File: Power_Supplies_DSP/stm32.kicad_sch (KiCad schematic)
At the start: 47 parts, among them J1 PINHD_1x10_Male, J2 SBH11-PBPC-D10-ST-BK, J4 PINHD_1x10_Male, J5 PINHD_1x2_Female, J6 PINHD_1x10_Female, U2 STM32H755ZIT6, U3 PEC11R-4030F-N0024, X3 NX3215SA-32.768K, X4 NX2016SA-32MHZ

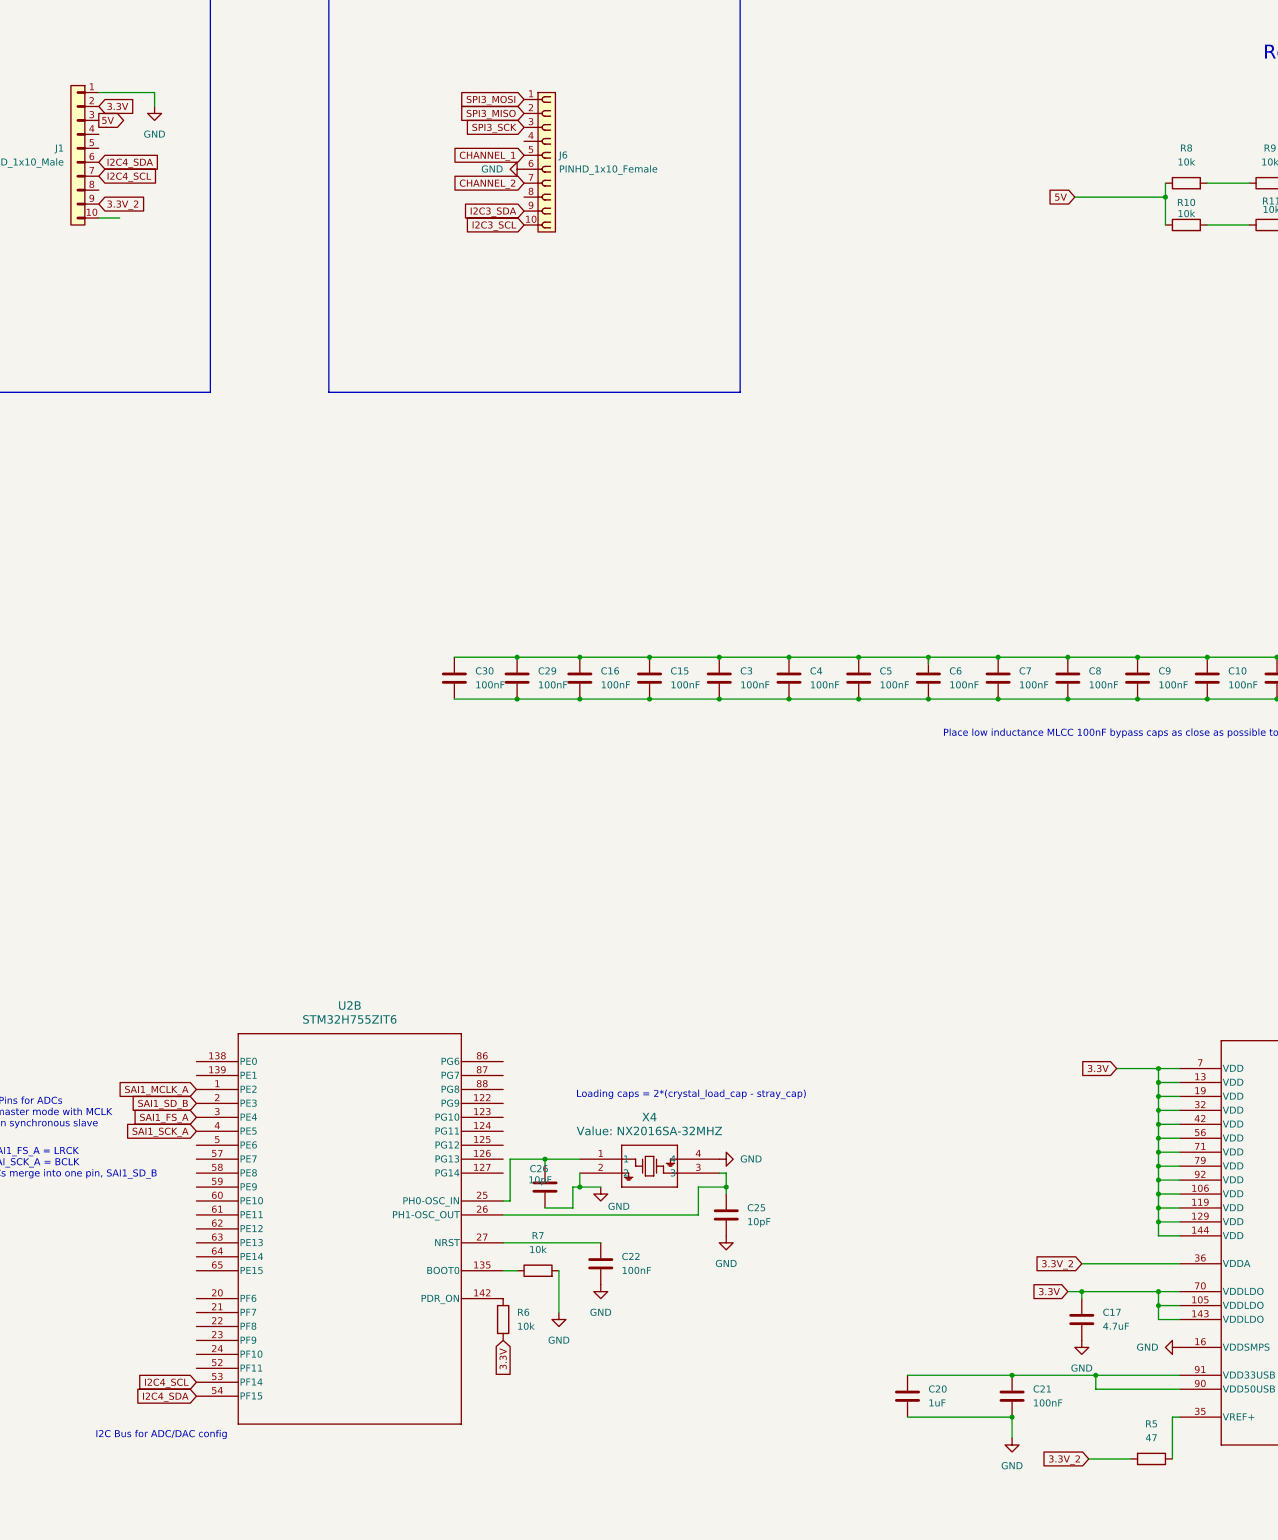
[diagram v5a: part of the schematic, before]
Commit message: fixed an oopsie w/ 3.3V on mcu board
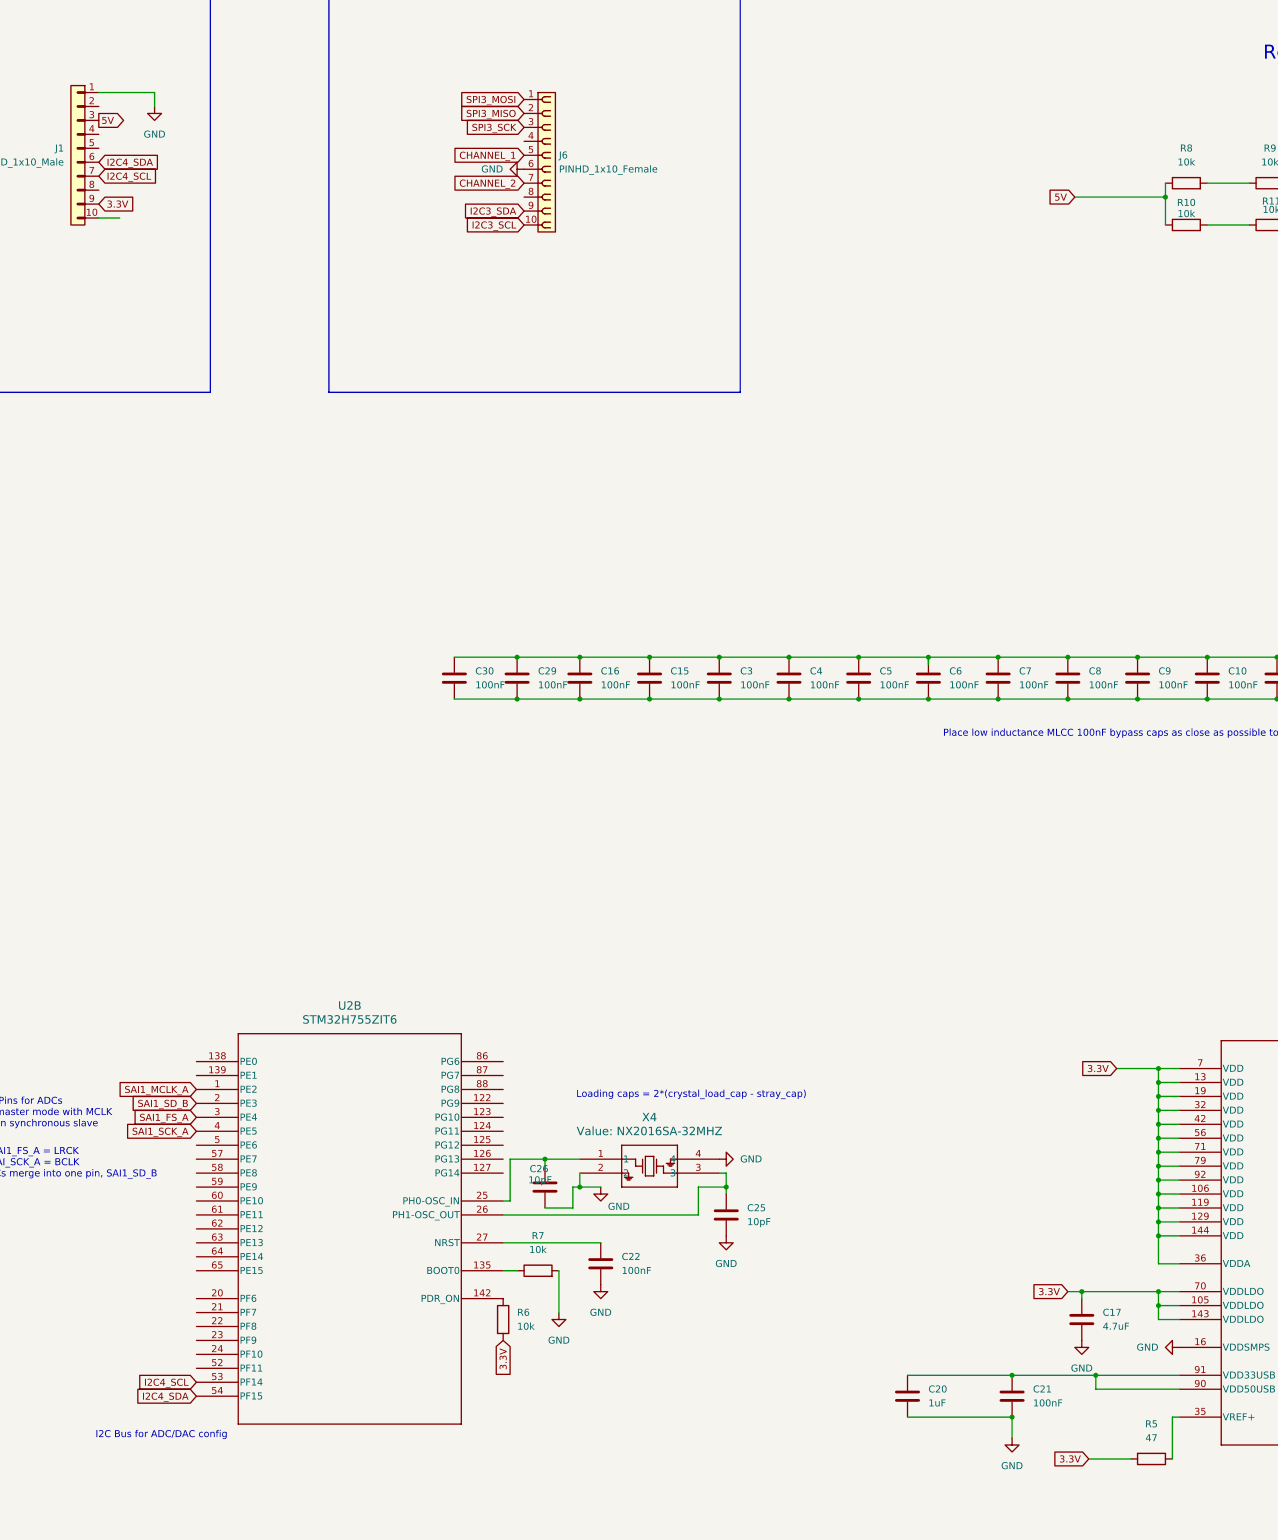
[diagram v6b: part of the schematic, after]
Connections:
- net 3.3V_2 is gone; now on net 3.3V: J1.9, R5.2, U2.36 (VDDA)
- net 3.3V: no longer J1.2
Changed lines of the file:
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@@
 	)
 	(junction
+		(at 464.82 269.24)
+		(diameter 0)
+		(color 0 0 0 0)
+	)
+	(junction
 		(at 359.41 163.83)
 		(diameter 0)
@@
 	(wire
 		(pts
-			(xy 450.85 274.32) (xy 468.63 274.32)
-		)
-		(stroke
-			(width 0)
-			(type default)
-		)
-	)
-	(wire
-		(pts
 			(xy 524.51 254) (xy 537.21 254)
 		)
@@
 	(wire
 		(pts
+			(xy 464.82 274.32) (xy 464.82 269.24)
+		)
+		(stroke
+			(width 0)
+			(type default)
+		)
+	)
+	(wire
+		(pts
 			(xy 527.05 302.26) (xy 524.51 302.26)
 		)
@@
 	(wire
 		(pts
+			(xy 468.63 274.32) (xy 464.82 274.32)
+		)
+		(stroke
+			(width 0)
+			(type default)
+		)
+	)
+	(wire
+		(pts
 			(xy 537.21 254) (xy 537.21 256.54)
 		)
@@
 		)
 	)
-	(global_label "3.3V"
-		(shape input)
-		(at 271.78 63.5 0)
-		(fields_autoplaced yes)
-		(effects
-			(font
-				(size 1.27 1.27)
-			)
-			(justify left)
-		)
-		(property "Intersheetrefs" "${INTERSHEET_REFS}"
-			(at 278.8776 63.5 0)
-			(effects
-				(font
-					(size 1.27 1.27)
-				)
-				(justify left)
-				(hide yes)
-			)
-		)
-	)
 	(global_label "SWDIO"
 		(shape input)
@@
 		)
 	)
-	(global_label "3.3V_2"
+	(global_label "JTDO_SWO"
 		(shape input)
-		(at 452.12 309.88 180)
+		(at 97.79 287.02 180)
 		(fields_autoplaced yes)
 		(effects
@@
 		)
 		(property "Intersheetrefs" "${INTERSHEET_REFS}"
-			(at 442.8453 309.88 0)
+			(at 85.3101 287.02 0)
 			(effects
 				(font
@@
 		)
 	)
-	(global_label "JTDO_SWO"
+	(global_label "JTDI"
 		(shape input)
-		(at 97.79 287.02 180)
+		(at 97.79 274.32 180)
 		(fields_autoplaced yes)
 		(effects
@@
 		)
 		(property "Intersheetrefs" "${INTERSHEET_REFS}"
-			(at 85.3101 287.02 0)
+			(at 90.9948 274.32 0)
 			(effects
 				(font
@@
 		)
 	)
-	(global_label "JTDI"
+	(global_label "3.3V"
 		(shape input)
-		(at 97.79 274.32 180)
+		(at 452.12 309.88 180)
 		(fields_autoplaced yes)
 		(effects
@@
 		)
 		(property "Intersheetrefs" "${INTERSHEET_REFS}"
-			(at 90.9948 274.32 0)
+			(at 445.0224 309.88 0)
 			(effects
 				(font
@@
 		)
 	)
-	(global_label "3.3V_2"
-		(shape input)
-		(at 450.85 274.32 180)
-		(fields_autoplaced yes)
-		(effects
-			(font
-				(size 1.27 1.27)
-			)
-			(justify right)
-		)
-		(property "Intersheetrefs" "${INTERSHEET_REFS}"
-			(at 441.5753 274.32 0)
-			(effects
-				(font
-					(size 1.27 1.27)
-				)
-				(justify right)
-				(hide yes)
-			)
-		)
-	)
 	(global_label "SAI2_FS_B"
 		(shape input)
@@
 		)
 	)
-	(global_label "3.3V_2"
+	(global_label "3.3V"
 		(shape input)
 		(at 271.78 81.28 0)
@@
 		)
 		(property "Intersheetrefs" "${INTERSHEET_REFS}"
-			(at 281.0547 81.28 0)
+			(at 278.8776 81.28 0)
 			(effects
 				(font

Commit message: stuff i may or may not have done to order these things
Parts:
- removed J2: SBH11-PBPC-D10-ST-BK, SamacSys_Parts:FTSH-110-XX-YYY-DV-K, symbol SDLibrary:SBH11-PBPC-D10-ST-BK
- removed U3: PEC11R-4030F-N0024, SamacSys_Parts:PEC11R4030FN0024, symbol SamacSys_Parts:PEC11R-4030F-N0024
- added J7: SBH11-PBPC-D10-ST-BK, SamacSys_Parts:SHDR20W64P254_2X10_2794X910X880P, symbol SamacSys_Parts:SBH11-PBPC-D10-ST-BK
- X3: footprint Inductor_SMD:L_6.3x6.3_H3 -> SamacSys_Parts:NX3215SA32768KSTDMUA8
- X4: footprint SamacSys_Parts:FA-238_EPS -> SamacSys_Parts:NX2016SA32MHZEXS00ACS06654
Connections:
- net 3.3V: now also J7.1, J7.2
- net GND: now also R13.1, R14.1, R15.1, J7.10, J7.12, J7.14, J7.16, J7.18, J7.20, J7.4, J7.6, J7.8; no longer R13.2, R14.2, R15.2
- net JTDI: now also J7.5
- net JTDO_SWO: now also J7.13
- net JTRST: now also J7.3
- net SWCLK: now also J7.9
- net SWDIO: now also J7.7
- new net: J7.11, R13.2
- new net: J7.17, R14.2
- new net: J7.19, R15.2
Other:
- moved on the sheet: R13, R14, R15

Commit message: fixed a lot of stuff
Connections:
- net 5V is gone; now on net 3.3V: J1.3, R10.1, R8.1
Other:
- note added: "SAI1_FS_A = LRCK SAI_SCK_A = BCLK Both Douts of ADCs (DIN) merge into one pin, SAI1_SD_B"
- note added: "SAI2_SCK_B = BCLK SAI2_FS-B = LRCK SAI2_SD_B = DATA"
- note removed: "SAI1_FS_A = LRCK SAI_SCK_A = BCLK Both Douts of ADCs merge into one pin, SAI1_SD_B"
- note removed: "SAI2_SCK_B = BCLK SAI2_FS-B = LRCK SAI2_SD_B = DIN"
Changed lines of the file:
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@@
 		)
 	)
-	(text "SAI2_SCK_B = BCLK\nSAI2_FS-B = LRCK\nSAI2_SD_B = DIN"
+	(text "SAI2_SCK_B = BCLK\nSAI2_FS-B = LRCK\nSAI2_SD_B = DATA"
 		(exclude_from_sim no)
 		(at 67.31 244.094 0)
@@
 		)
 	)
-	(text "SAI1_FS_A = LRCK\nSAI_SCK_A = BCLK\nBoth Douts of ADCs merge into one pin, SAI1_SD_B"
+	(text "SAI1_FS_A = LRCK\nSAI_SCK_A = BCLK\nBoth Douts of ADCs (DIN) merge into one pin, SAI1_SD_B"
 		(exclude_from_sim no)
 		(at 260.096 256.032 0)
@@
 		)
 	)
-	(global_label "5V"
+	(global_label "3.3V"
 		(shape input)
 		(at 449.58 80.01 180)
@@
 		)
 		(property "Intersheetrefs" "${INTERSHEET_REFS}"
-			(at 444.2967 80.01 0)
+			(at 442.4824 80.01 0)
 			(effects
 				(font
@@
 		)
 	)
-	(global_label "5V"
+	(global_label "3.3V"
 		(shape output)
 		(at 271.78 66.04 0)
@@
 		)
 		(property "Intersheetrefs" "${INTERSHEET_REFS}"
-			(at 277.0633 66.04 0)
-			(effects
-				(font
+			(at 278.8776 66.04 0)
+			(effects
+				(font
